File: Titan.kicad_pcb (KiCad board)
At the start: 4 copper layers, 60 x 115 mm, 155 parts, among them J1 USB_B_Micro, J10 PWM1, J11 SPI SLAVE, J12 IO Conn 2, J13 IO Conn 1, J14 ADC EXT, J15 PWM2, J2 USB_B_Micro, J3 Uart 1, J4 Bat Conn, J5 Debug, J6 Uart 2, J7 SPI AUX MASTER, J8 S3B-ZR(LF)(SN), J9 S3B-ZR(LF)(SN), Q1 NDS332P, Q2 NDS332P, SW1 SW_Push, SW2 SW_DPDT_x2, U1 FT230XS, U2 SR10S3V3, U3 STM32F413VGTx, U4 CY15B104Q, U5 MPU-6050, U6 FT230XS, U7 XBEE3Micro, U8 MPU-6050

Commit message: First commit of TitanV2
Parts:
- removed C2: 470uF, Titan:T59EE477M016C0025
- removed J10: PWM1, Footprint:HDRV8W85P254_8X1_2078X650X1000
- removed J11: SPI SLAVE, Connector_PinHeader_2.54mm:PinHeader_2x03_P2.54mm_Vertical
- removed J12: IO Conn 2, Connector_PinHeader_2.54mm:PinHeader_2x05_P2.54mm_Vertical
- removed J13: IO Conn 1, Connector_PinHeader_2.54mm:PinHeader_2x07_P2.54mm_Vertical
- removed J14: ADC EXT, Connector_PinHeader_2.54mm:PinHeader_2x03_P2.54mm_Vertical
- removed J15: PWM2, Footprint:HDRV8W85P254_8X1_2078X650X1000
- removed J6: Uart 2, TerminalBlock_TE-Connectivity:TerminalBlock_TE_282834-4_1x04_P2.54mm_Horizontal
- removed J7: SPI AUX MASTER, Connector_PinHeader_2.54mm:PinHeader_2x03_P2.54mm_Vertical
- removed L1: 1231AS-H-6R4M=P3, Footprint:IND_1231AS-H-6R4M=P3
- removed R1: 330, Resistor_SMD:R_0603_1608Metric_Pad1.05x0.95mm_HandSolder
- removed R16, R17, R19, R39, R40, R41, R42, R8: 220, Resistor_SMD:R_0603_1608Metric_Pad1.05x0.95mm_HandSolder
- removed R18, R63, R7: 0, Resistor_SMD:R_0603_1608Metric_Pad1.05x0.95mm_HandSolder
- removed R4, R5: 10k, Resistor_SMD:R_0603_1608Metric_Pad1.05x0.95mm_HandSolder
- removed R43, R44, R45, R46, R47, R48, R49, R50, R51, R52, R53, R54, R55, R56, R57, R58: 1K, Resistor_SMD:R_0603_1608Metric_Pad1.05x0.95mm_HandSolder
- removed SW1: SW_Push, Titan:TL3301AF160QG
- removed SW2: SW_DPDT_x2, Titan:CASD20
- removed TP1, TP2: TestPoint, TestPoint:TestPoint_Pad_1.5x1.5mm
- added S1: Reset button, digikey-footprints:Switch_Tactile_SMD_4.5x4.5mm_TL3315NF160Q, F.Cu at (127.7, 92.1)
- C1: value 470uF -> 2.2uF; footprint Titan:T59EE477M016C0025 -> Capacitor_SMD:C_0603_1608Metric_Pad1.08x0.95mm_HandSolder; moved to B.Cu
- C10, C12, C15, C17, C18, C20, C21, C22, C23, C24, C25, C26, C3, C35, C36, C4, C5, C6, C7, C8, C9: footprint Capacitor_SMD:C_0603_1608Metric_Pad1.05x0.95mm_HandSolder -> Capacitor_SMD:C_0603_1608Metric_Pad1.08x0.95mm_HandSolder
- C11, C19, C29, C30, C31, C32, C33, C55, C56: footprint Capacitor_SMD:C_0603_1608Metric_Pad1.05x0.95mm_HandSolder -> Capacitor_SMD:C_0603_1608Metric_Pad1.08x0.95mm_HandSolder; moved to F.Cu
- C13, C14, C16, C27, C28: footprint Capacitor_SMD:C_0603_1608Metric_Pad1.05x0.95mm_HandSolder -> Capacitor_SMD:C_0603_1608Metric_Pad1.08x0.95mm_HandSolder; moved to B.Cu
- C34: value 22uF -> 2.2uF; footprint Capacitor_SMD:C_0603_1608Metric_Pad1.05x0.95mm_HandSolder -> Capacitor_SMD:C_0603_1608Metric_Pad1.08x0.95mm_HandSolder; moved to B.Cu
- D1, U6: moved to B.Cu
- D2: value PWR_ON -> D_Schottky; footprint LED_SMD:LED_0805_2012Metric_Pad1.15x1.40mm_HandSolder -> Diode_SMD:D_SOD-123; moved to B.Cu
- FB1: footprint Resistor_SMD:R_0805_2012Metric_Pad1.15x1.40mm_HandSolder -> Resistor_SMD:R_0805_2012Metric_Pad1.20x1.40mm_HandSolder; moved to F.Cu
- J3: value Uart 1 -> PWR CON
- J4: value Bat Conn -> Screw_Terminal_01x08; footprint digikey-footprints:Terminal_Block_D1.3mm_P5mm -> Footprint:HDRV8W85P254_8X1_2078X650X1000
- Q1, Q2: footprint digikey-footprints:SOT-23-3 -> Titan:SOT-23-3
- R10, R11, R12, R13, R14, R15, R2, R20, R21, R22, R23, R3, R32, R33, R36, R37, R38, R59, R60, R61, R62, R72, R9: footprint Resistor_SMD:R_0603_1608Metric_Pad1.05x0.95mm_HandSolder -> Resistor_SMD:R_0603_1608Metric_Pad0.98x0.95mm_HandSolder
- R24, R25, R26, R27, R28, R29, R30, R31, R68, R69, R70, R71: footprint Resistor_SMD:R_0603_1608Metric_Pad1.05x0.95mm_HandSolder -> Resistor_SMD:R_0603_1608Metric_Pad0.98x0.95mm_HandSolder; moved to B.Cu
- R34, R35, R6: footprint Resistor_SMD:R_0603_1608Metric_Pad1.05x0.95mm_HandSolder -> Resistor_SMD:R_0603_1608Metric_Pad0.98x0.95mm_HandSolder; moved to F.Cu
- U2: value SR10S3V3 -> ST730M33R; footprint Titan:SR10S3V3 -> Package_TO_SOT_SMD:SOT-23-5_HandSoldering; moved to B.Cu
- U4, U8, XTAL1: moved to F.Cu
- moved R34 96.9 mm to (149.4, 106.5), turned to 90 degrees
- moved R35 93.6 mm to (147.9, 106.5), turned to 90 degrees
- moved H1 93.5 mm to (155.0, 100.0)
- moved J8 93.2 mm to (156.7, 106.4), turned to 270 degrees
- moved C11 89.8 mm to (147.9, 95.4)
- moved D15 87.4 mm to (144.3, 106.2)
- moved R14 87.3 mm to (144.3, 110.0)
- moved C31 86.4 mm to (146.4, 95.4)
- moved U8 86.2 mm to (147.1, 99.8), turned to 180 degrees
- moved H4 84.4 mm to (125.0, 100.0)
- moved J9 84.1 mm to (123.3, 109.6)
- moved D14 83.5 mm to (142.2, 106.2)
- moved C33 83.4 mm to (145.6, 103.3)
- moved R13 83.4 mm to (142.2, 110.0)
- moved R6 83.1 mm to (144.9, 95.4)
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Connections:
- D2 pad 1: Net-(D2-Pad1) -> Net-(C1-Pad1)
- D2 pad 2: VDD_MCU -> /VBUS_COM
- J1 pad 1: Net-(J1-Pad1) -> /VBUS_COM
- J3 pad 1: VDD_MCU -> GND
- J3 pad 2: GND -> VDD_MCU
- J3 pad 3: Net-(J3-Pad3) -> GND
- J3 pad 4: Net-(J3-Pad4) -> Net-(D1-Pad2)
- J4 pad 1: Net-(D1-Pad2) -> /PWM_1
- J4 pad 2: GND -> /PWM_2
- J8 pad 3: Net-(J8-Pad3) -> /UART_RC_1_RX
- J9 pad 3: Net-(J9-Pad3) -> /UART_RC_2_RX
- R59 pad 1: GND -> VDD_MCU
- R70 pad 1: Net-(J1-Pad1) -> /VBUS_COM
- U2 pad 1: Net-(C2-Pad1) -> VDD_MCU
- U2 pad 3: VDD_MCU -> Net-(C1-Pad1)
- U3 pad 12: Net-(R7-Pad1) -> Net-(C29-Pad1)
- U3 pad 13: Net-(R63-Pad1) -> Net-(C30-Pad1)
- U3 pad 17: SPI_SLAVE_MISO -> (no net)
- U3 pad 18: SPI_SLAVE_MOSI -> (no net)
- U3 pad 2: /UART_RC_1_TX -> (no net)
- U3 pad 21: Net-(R18-Pad1) -> VDDA_MCU
- U3 pad 24: ADC_1 -> (no net)
- U3 pad 25: ADC_2 -> (no net)
- U3 pad 26: ADC_3 -> (no net)
- U3 pad 33: /IO_12 -> (no net)
- U3 pad 35: /PWM_5 -> (no net)
- U3 pad 36: /PWM_6 -> (no net)
- U3 pad 37: BOOT1 -> (no net)
- U3 pad 38: /IO_1 -> (no net)
- U3 pad 39: /IO_2 -> (no net)
- U3 pad 4: SPI_AUX_MISO -> (no net)
- U3 pad 41: /IO_3 -> (no net)
- U3 pad 42: SPI_AUX_NSS -> (no net)
- U3 pad 43: SPI_AUX_SCK -> (no net)
- U3 pad 46: /IO_4 -> (no net)
- U3 pad 5: SPI_AUX_MOSI -> (no net)
- U3 pad 51: SPI_SLAVE_NSS -> (no net)
- U3 pad 52: SPI_SLAVE_SCK -> (no net)
- U3 pad 54: /IO_11 -> (no net)
- U3 pad 56: /IO_5 -> (no net)
- U3 pad 57: /IO_6 -> (no net)
- U3 pad 59: /IO_7 -> (no net)
- U3 pad 60: /IO_8 -> (no net)
- U3 pad 65: /IO_13 -> (no net)
- U3 pad 66: /IO_14 -> (no net)
- U3 pad 67: /IO_9 -> (no net)
- U3 pad 78: /IO_15 -> (no net)
- U3 pad 79: /IO_10 -> (no net)
- U3 pad 86: /UART_RC_2_TX -> (no net)
- U3 pad 89: /IO_16 -> (no net)
- U3 pad 90: /PWM_7 -> (no net)
- U3 pad 91: /PWM_8 -> (no net)
- U3 pad 94: BOOT0 -> GND
- U3 pad 97: /UART_MOTOR_1_RX -> (no net)
- U3 pad 98: /UART_MOTOR_1_TX -> (no net)
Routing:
- net GND: track 253.7 -> 0.00 mm, vias 44 -> 0
- net VDD_MCU: track 139.1 -> 0.00 mm, vias 31 -> 0
- net /IMU2_INT: track 88.5 -> 0.00 mm, vias 1 -> 0
- net /nRESET: track 72.8 -> 0.00 mm, vias 2 -> 0
- net /I2C_SDA_IMU: track 69.1 -> 0.00 mm, vias 4 -> 0
- net /I2C_SCL_IMU: track 61.1 -> 0.00 mm, vias 4 -> 0
- net Net-(C28-Pad2): track 59.6 -> 0.00 mm, vias 5 -> 0
- net /UART_COM_CTS: track 59.4 -> 0.00 mm, vias 2 -> 0
- net /PWM_8: track 57.5 -> 0.00 mm
- net SPI_SLAVE_NSS: track 56.2 -> 0.00 mm, vias 2 -> 0
- net /UART_COM_TX: track 55.3 -> 0.00 mm, vias 2 -> 0
- net SPI_SLAVE_SCK: track 54.1 -> 0.00 mm, vias 2 -> 0
- net /UART_COM_RX: track 53.3 -> 0.00 mm
- net /UART_COM_RTS: track 53.2 -> 0.00 mm, vias 2 -> 0
- net /ADC_BAT: track 53.0 -> 0.00 mm, vias 5 -> 0
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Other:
- board size 60 x 115 mm -> 45 x 72.5 mm
- board text removed: "+"
- board text removed: "-"
- board text removed: "1"
- board text removed: "2"
- board text removed: "3"
- board text removed: "4"
- board text removed: "5"
- board text removed: "6"
- board text removed: "7"
- board text removed: "8"
- board text removed: "ADC"
- board text removed: "COM"
- board text removed: "DBG"
- board text removed: "Error"
- board text removed: "Fatal"
- board text removed: "G"
- board text removed: "GND"
- board text removed: "HB"
- board text removed: "IO CONN 1"
- board text removed: "IO CONN 2"
- board text removed: "Input: 4,75-18V"
- board text removed: "Mode"
- board text removed: "PWM"
- board text removed: "RX"
- board text removed: "SP"
- board text removed: "SPI MASTER"
- board text removed: "SPI SLAVE"
- board text removed: "Status"
- board text removed: "TX"
- board text removed: "Titan V1.0"
- board text removed: "VDD"

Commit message: First commit of TitanV2
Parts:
- C10, C18, C19: moved to B.Cu
- moved C3 23.9 mm to (151.4, 82.1), turned to 90 degrees
- moved C10 16.0 mm to (144.6, 82.7), turned to 270 degrees
- moved C19 12.6 mm to (139.2, 78.7)
- moved C18 12.1 mm to (139.2, 80.2)
- moved C13 10.4 mm to (158.2, 84.9), turned to 0 degrees
- moved C27 8.68 mm to (150.9, 95.0), turned to 180 degrees
- moved C28 8.54 mm to (147.3, 74.9), turned to 180 degrees
- moved C56 7.71 mm to (126.7, 65.5), turned to 0 degrees
- moved C55 7.53 mm to (138.9, 65.0), turned to 270 degrees
- moved C12 7.14 mm to (158.2, 90.0), turned to 180 degrees
- moved R30 6.71 mm to (147.1, 86.7), turned to 0 degrees
- moved C4 5.88 mm to (137.7, 72.5), turned to 90 degrees
- moved C16 5.63 mm to (136.4, 95.2)
- moved R24 4.98 mm to (147.1, 93.7), turned to 0 degrees
- moved U4 4.85 mm to (133.3, 66.3), turned to 0 degrees
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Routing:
- net GND: track 0.00 -> 181.7 mm, vias 0 -> 35
- net VDD_MCU: track 0.00 -> 106.7 mm, vias 0 -> 28
- net /nRESET: track 0.00 -> 81.4 mm, vias 0 -> 3
- net /UART_COM_RX: track 0.00 -> 68.2 mm
- net Net-(C28-Pad2): track 0.00 -> 65.1 mm, vias 0 -> 2
- net /RC_2_PWR_CTRL: track 0.00 -> 61.9 mm, vias 0 -> 4
- net /UART_RC_2_RX: track 0.00 -> 58.0 mm, vias 0 -> 3
- net /UART_COM_RTS: track 0.00 -> 57.7 mm
- net /VBUS_COM: track 0.00 -> 47.5 mm, vias 0 -> 1
- net /UART_COM_TX: track 0.00 -> 44.6 mm, vias 0 -> 2
- net /IMU1_INT: track 0.00 -> 42.2 mm, vias 0 -> 2
- net /SPI_MEM_MOSI: track 0.00 -> 41.3 mm
- net /I2C_SDA_IMU: track 0.00 -> 40.9 mm
- net /UART_COM_CTS: track 0.00 -> 39.8 mm, vias 0 -> 2
- net /I2C_SCL_IMU: track 0.00 -> 38.1 mm, vias 0 -> 4
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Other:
- net class Default: clearance 0.2 -> 0.15
- rule trace_clearance: 0.2 -> 0.15

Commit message: As ordered from Aisler.
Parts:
- S1: footprint digikey-footprints:Switch_Tactile_SMD_4.5x4.5mm_TL3315NF160Q -> digikey-footprints:Switch_Tactile_SMD_6x6mm
- U2: value ST730M33R -> ST732M33R
- U4: footprint Footprint:SOIC127P523X800X203-8N -> Package_SO:SOP-8_3.9x4.9mm_P1.27mm
- moved S1 17.5 mm to (130.9, 74.9), turned to 45 degrees
- moved C15 12.8 mm to (126.2, 79.8), turned to 135 degrees
- moved U2 5.34 mm to (130.5, 74.9), turned to 270 degrees
- moved C1 4.66 mm to (133.5, 72.9), turned to 90 degrees
- moved C34 4.31 mm to (130.6, 71.2), turned to 180 degrees
- moved C4 1.94 mm to (139.6, 72.7)
- moved C56 1.18 mm to (127.9, 65.8)
- moved U4 0.61 mm to (133.5, 65.7)
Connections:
- U2 pad 1: VDD_MCU -> GND
- U2 pad 2: GND -> Net-(C1-Pad1)
- U2 pad 3: Net-(C1-Pad1) -> VDD_MCU
- U2 pad 5: Net-(C1-Pad1) -> (no net)
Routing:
- net /nRESET: track 81.4 -> 106.0 mm, vias 3 -> 4
- net GND: track 181.7 -> 196.1 mm, vias 35 -> 36
- net Net-(C1-Pad1): track 18.7 -> 12.4 mm
- net /VBUS_COM: track 47.5 -> 52.3 mm
- net /PWM_2: track 33.4 -> 37.4 mm
- net /SPI_MEM_NSS: track 23.0 -> 19.3 mm
- net /UART_COM_RX: track 68.2 -> 70.6 mm
- net /PWM_4: track 15.0 -> 17.1 mm
- net VDD_MCU: track 106.7 -> 108.5 mm, vias 28 -> 29
- net Net-(C28-Pad2): track 65.1 -> 66.6 mm
- net /SPI_MEM_SCK: track 14.2 -> 12.9 mm
- net /SPI_MEM_MISO: track 15.0 -> 15.9 mm
- net Net-(D6-Pad1): track 33.9 -> 34.9 mm
- net /UART_COM_TX: track 44.6 -> 43.8 mm
- net /RC_2_PWR_CTRL: track 61.9 -> 61.2 mm
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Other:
- board text added: "+"
- board text added: "-"
- board text added: "3.3v"
- board text added: "C Mode"
- board text added: "COM"
- board text added: "DBG"
- board text added: "Error"
- board text added: "Fatal"
- board text added: "G"
- board text added: "GND"
- board text added: "HB"
- board text added: "Input: 4,7 - 28V"
- board text added: "PWM 1"
- board text added: "PWM 2"
- board text added: "PWM 3"
- board text added: "PWM 4"
- board text added: "RX"
- board text added: "SP"
- board text added: "Status"
- board text added: "TX"

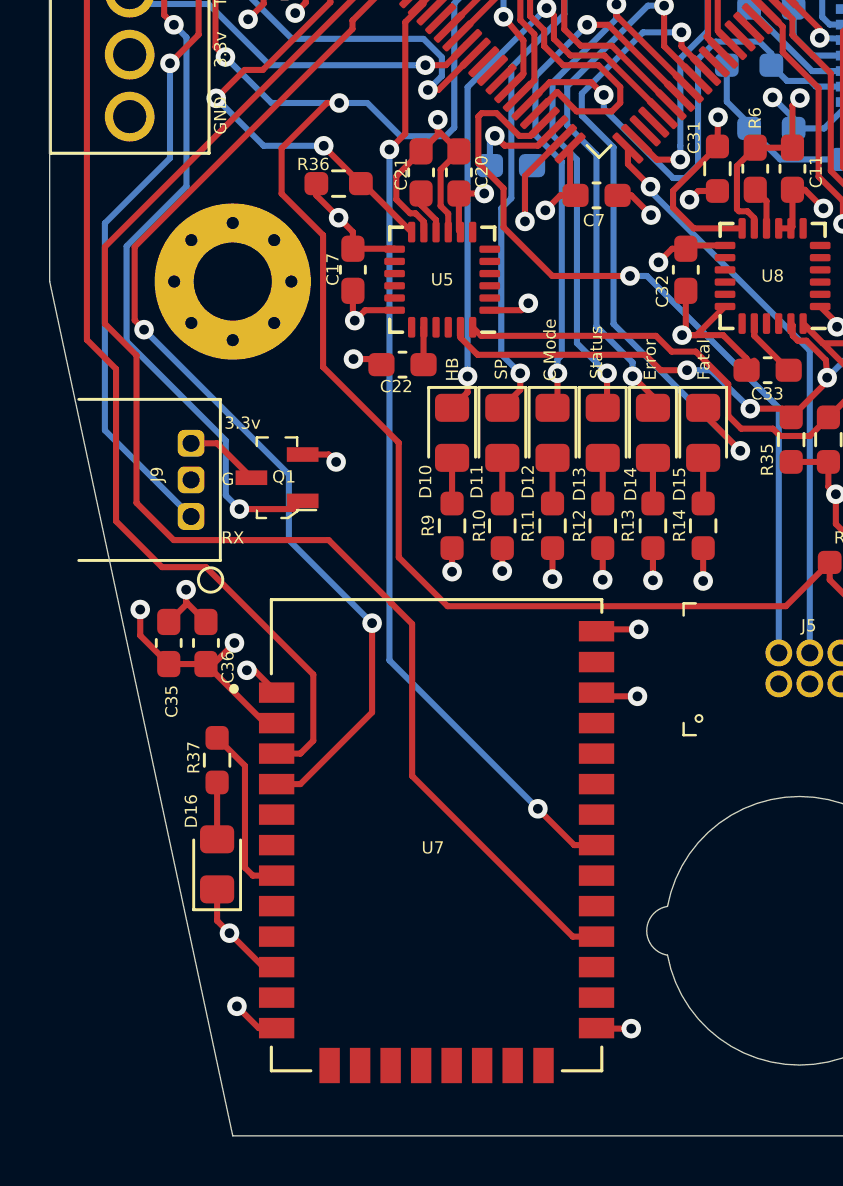
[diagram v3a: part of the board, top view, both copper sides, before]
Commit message: Update silkscreen.
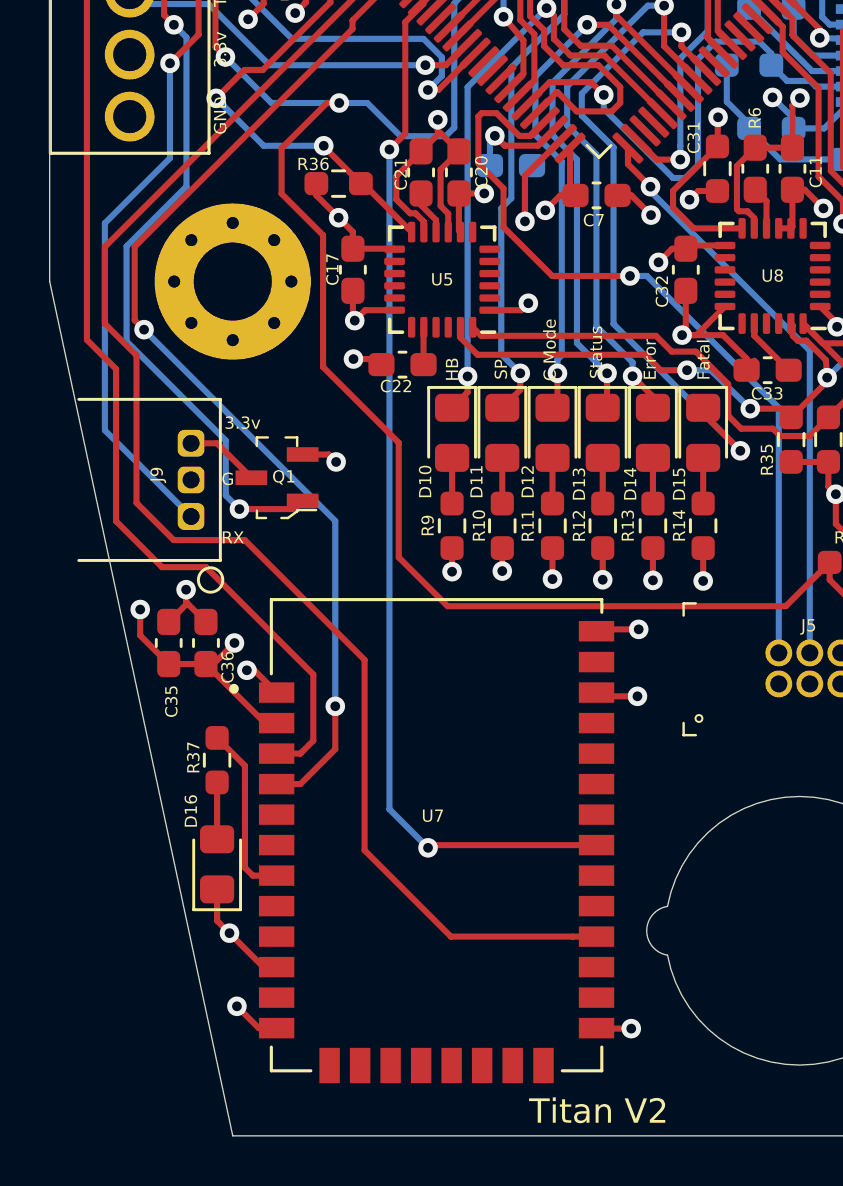
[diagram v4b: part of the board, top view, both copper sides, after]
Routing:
- net /UART_COM_CTS: track 39.2 -> 42.9 mm
- net /UART_COM_TX: track 43.8 -> 42.6 mm
- net /UART_COM_RTS: track 57.5 -> 58.4 mm
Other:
- board text added: "Titan V2"

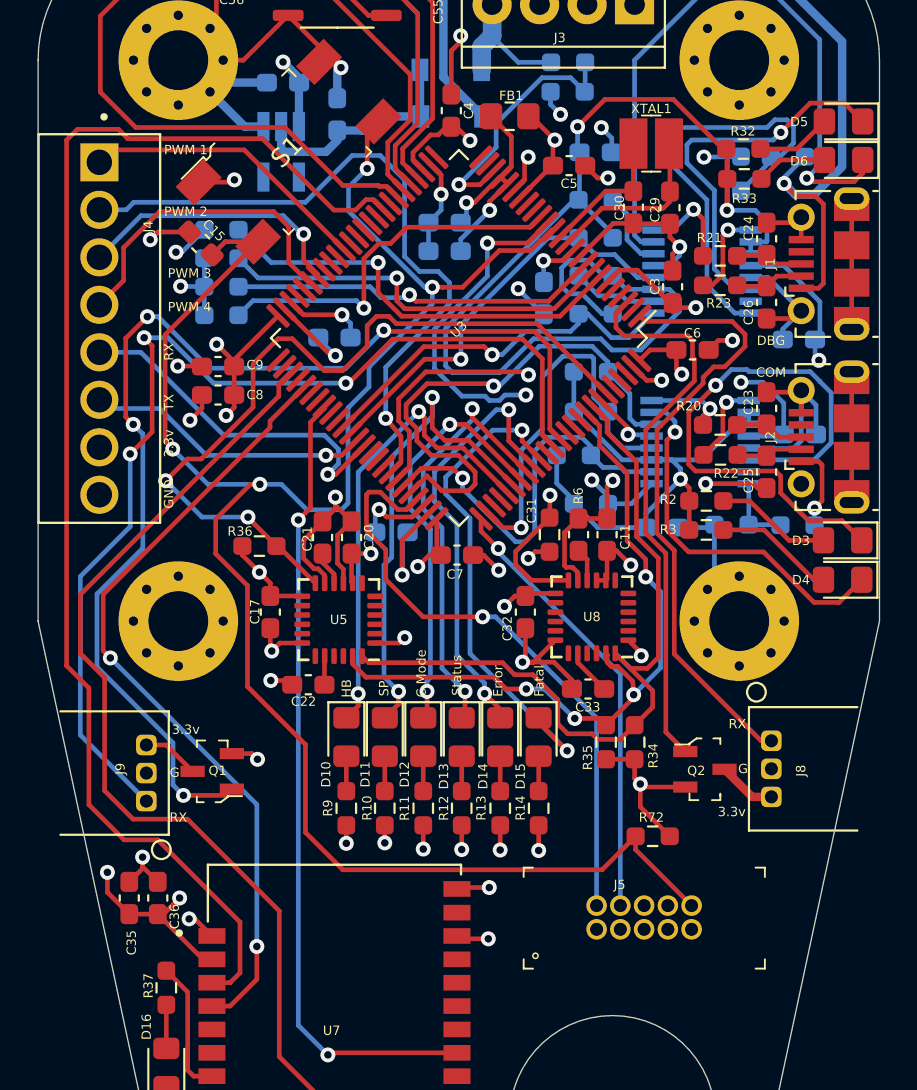
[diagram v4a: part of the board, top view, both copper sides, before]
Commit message: Made the copper pour slightly smaller and removed it around the antenna mount. Also corrected some silkscreen print.
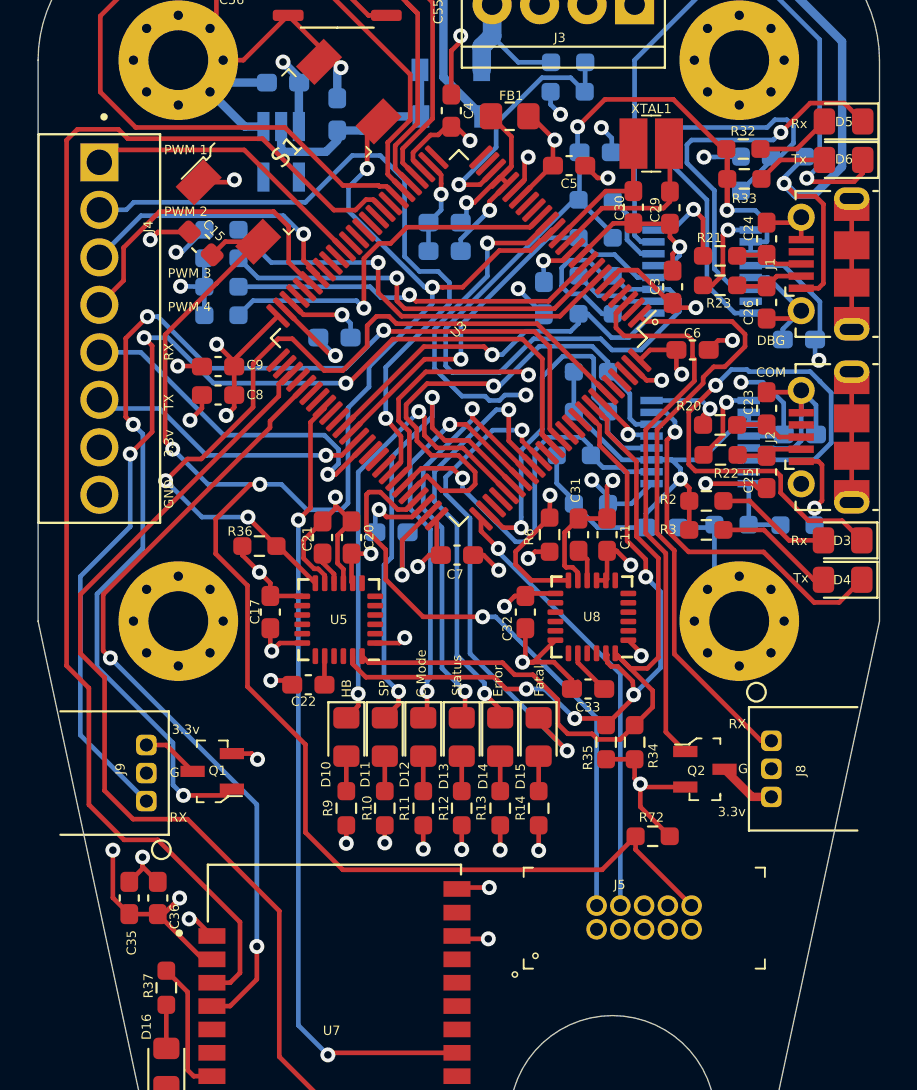
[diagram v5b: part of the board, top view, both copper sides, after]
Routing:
- net VDD_MCU: track 108.5 -> 109.6 mm
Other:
- board text added: "Rx"
- board text added: "Tx"

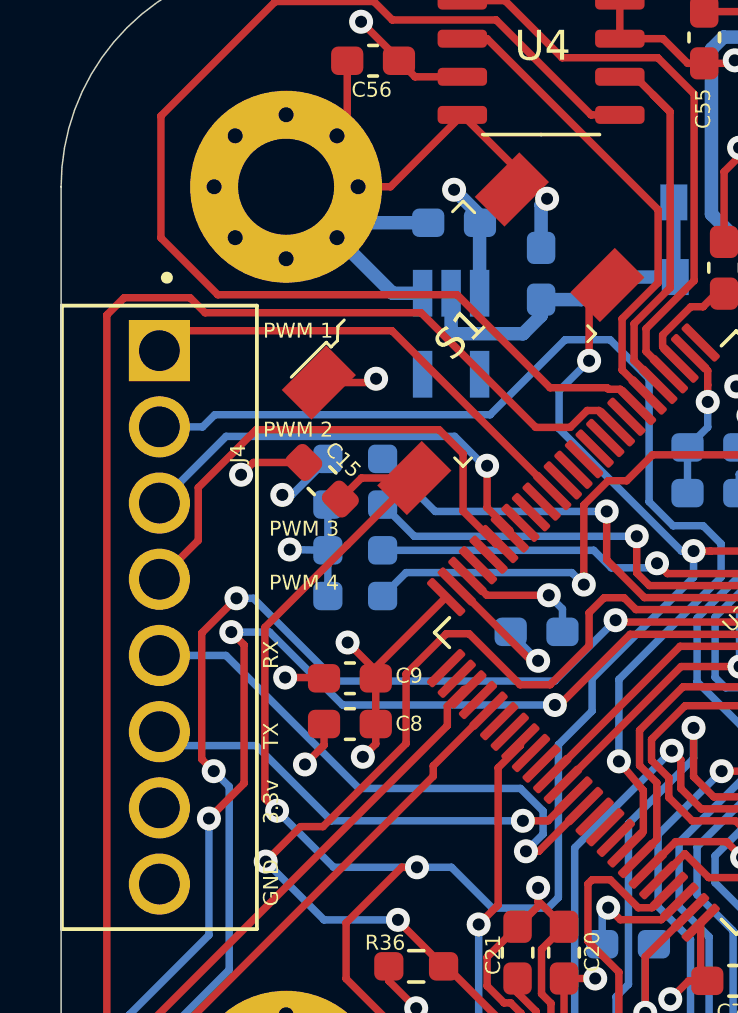
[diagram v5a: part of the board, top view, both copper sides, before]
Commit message: Added a 5V regulator and connector. This will make it possible to power newer rc receivers.
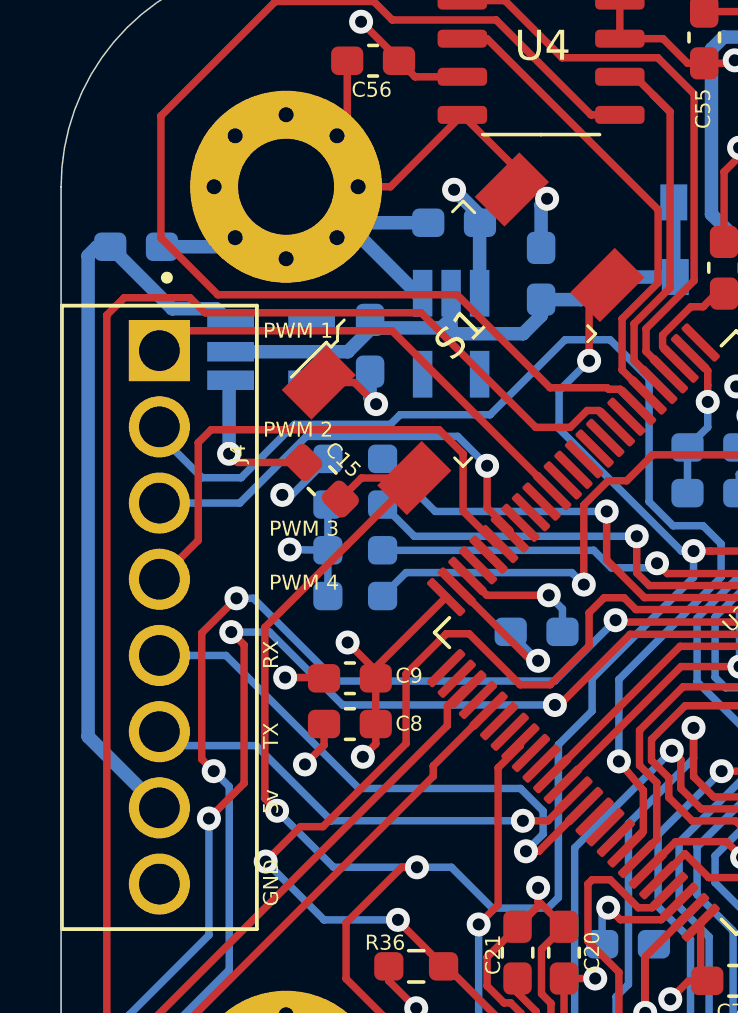
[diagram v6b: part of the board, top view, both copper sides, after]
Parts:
- added C2: 2.2uF, Capacitor_SMD:C_0603_1608Metric_Pad1.08x0.95mm_HandSolder, B.Cu at (127.8, 75.3)
- added C37: 2.2uF, Capacitor_SMD:C_0603_1608Metric_Pad1.08x0.95mm_HandSolder, B.Cu at (120.0, 72.0)
- added U9: ST732M50R, Package_TO_SOT_SMD:SOT-23-5_HandSoldering, B.Cu at (124.5, 75.5)
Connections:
- J4 pad 7: VDD_MCU -> +5V
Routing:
- net +5V: track 0.00 -> 25.4 mm
- net GND: track 196.1 -> 205.4 mm
- net Net-(C1-Pad1): track 12.4 -> 21.4 mm
- net /PWM_2: track 37.4 -> 38.9 mm
- net /PWM_4: track 17.1 -> 18.0 mm
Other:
- board text added: "5v"
